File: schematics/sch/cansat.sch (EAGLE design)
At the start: 39 parts

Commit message: cansat main board
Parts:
- removed BAT1IN5V, BAT1INGND, BAT1OUT+, BAT1OUTGND, BAT2IN5V, BAT2INGND, BAT2OUT+, BAT2OUTGND: (no value), pinhead:PINHD-1X1
- removed EXGPIO, EXSPI: (no value), pinhead:PINHD-1X4
- removed EXI2C, EXP1, EXP2, EXP3, EXUART: (no value), pinhead:PINHD-1X2
- removed GPSL: (no value), pinhead:PINHD-1X8
- removed USB: (no value), pinhead:PINHD-1X5
- added D1, D2: GF1, diode:GF1
- added GPS: (no value), pinhead:PINHD-1X4
- added SJ1, SJ2: (no value), jumper:SJ2WW
- C1, C2, C3, C4, C5, C6: device resistor:C-EU025-025X050 -> eagle-ltspice:CC1206
- R1, R2, R3, R4: value (none) -> 10k; device resistor:R-EU_0204/2V -> eagle-ltspice:RR1206
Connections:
- removed net USB5V: BAT1IN5V.1, BAT2IN5V.1, USB.1
- new net ENCODER1_ADC: SJ1.3, VOLTMETER.9
- new net ENCODER1_DIR: RASPIZERO.GPIO20, SJ1.1
- new net ENCODER2_ADC: SJ2.3, VOLTMETER.10
- new net ENCODER2_DIR: RASPIZERO.GPIO21, SJ2.1
- new net N$10: BATIN.1, D1.A
- new net N$11: BATIN.2, D2.A
- new net R_INT: RADIOR.3
- net 3.3V: now also 3.3V1.4, 3.3V2.4, GPS.2; no longer 3.3V1.1, 3.3V2.1, EXP1.1, EXP2.1, EXP3.1, GPSL.7
- net BAT1+: now also 3.3V1.2, D1.C; no longer 3.3V1.3, BAT1OUT+.1, BATIN.1
- net BAT2+: now also 3.3V2.2, D2.C; no longer 3.3V2.3, BAT2OUT+.1, BATIN.2
- net ENCODER1: now also SJ1.2; no longer RASPIZERO.GPIO20
- net ENCODER2: now also SJ2.2; no longer RASPIZERO.GPIO21
- net EX1: no longer EXGPIO.1
- net EX2: no longer EXGPIO.2
- net EX3: no longer EXGPIO.3
- net EX4: no longer EXGPIO.4
- net GND: now also 3.3V1.3, 3.3V2.3, GPS.1, R2.1; no longer 3.3V1.2, 3.3V2.2, BAT1INGND.1, BAT1OUTGND.1, BAT2INGND.1, BAT2OUTGND.1, EXP1.2, EXP2.2, EXP3.2, GPSL.8, USB.5, VOLTMETER.10, VOLTMETER.8
- net GPSTX: now also GPS.3; no longer GPSL.6
- net MISO: no longer EXSPI.1
- net MOSI: no longer EXSPI.2
- net N$1: now also R2.2, VOLTMETER.8; no longer R2.1, VOLTMETER.7
- net N$9: now also VOLTMETER.7; no longer VOLTMETER.9
- net RX: no longer EXUART.2
- net SCL: no longer EXI2C.2
- net SCLK: no longer EXSPI.3
- net SDA: no longer EXI2C.1
- net SHDN: now also 3.3V1.1, 3.3V2.1; no longer 3.3V1.4, 3.3V2.4
- net SS: no longer EXSPI.4
- net TX: no longer EXUART.1
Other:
- note removed: "BATTERY 1 CHARGER"
- note removed: "BATTERY 2 CHARGER"
- note removed: "CHARGERS"
- note removed: "USB INPUT"
- moved on the sheet: BATIN, R1, R2, R3, R4, RADIOR, VOLTMETER

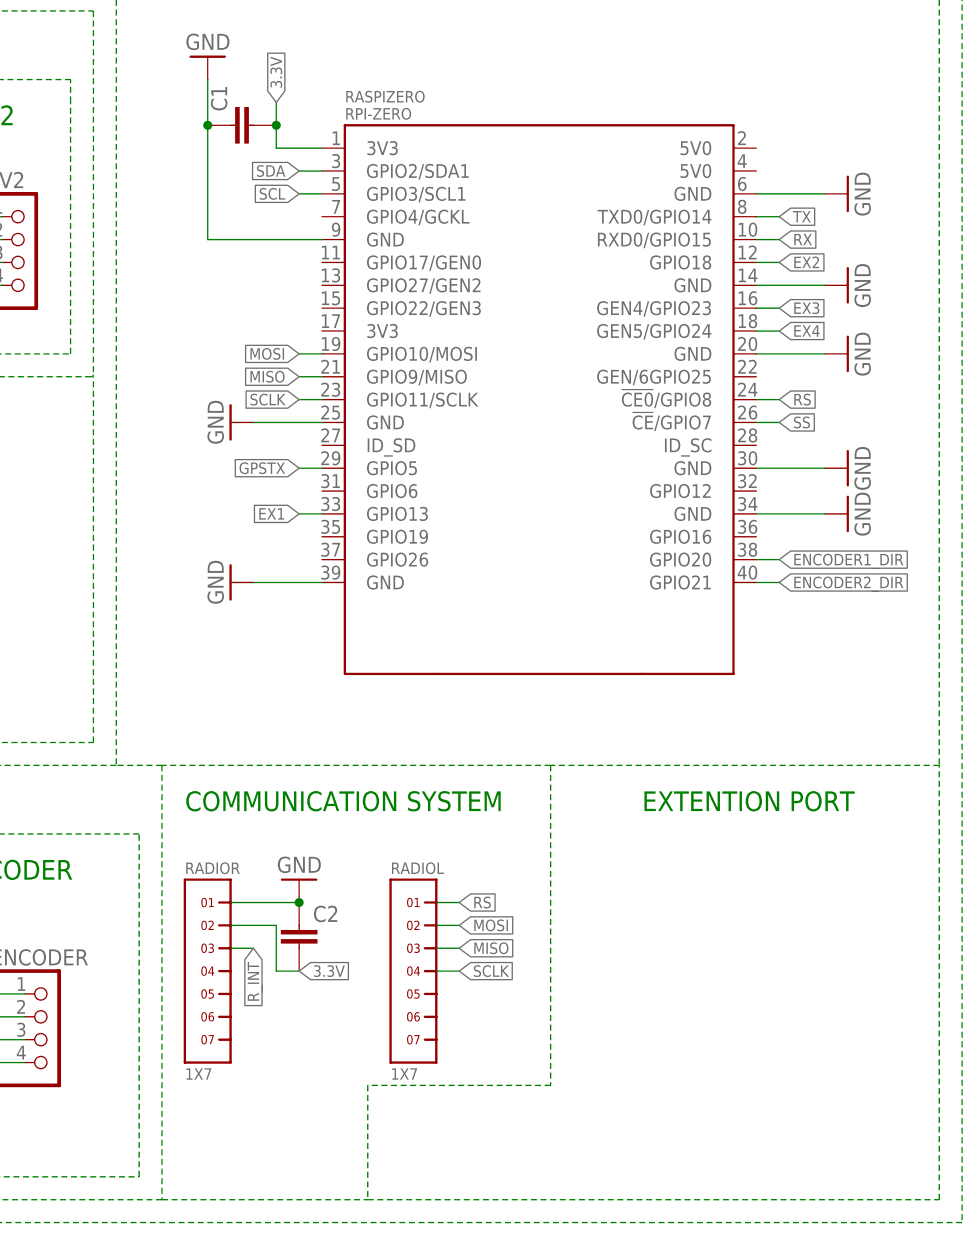
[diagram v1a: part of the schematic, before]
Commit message: cansat board fixed
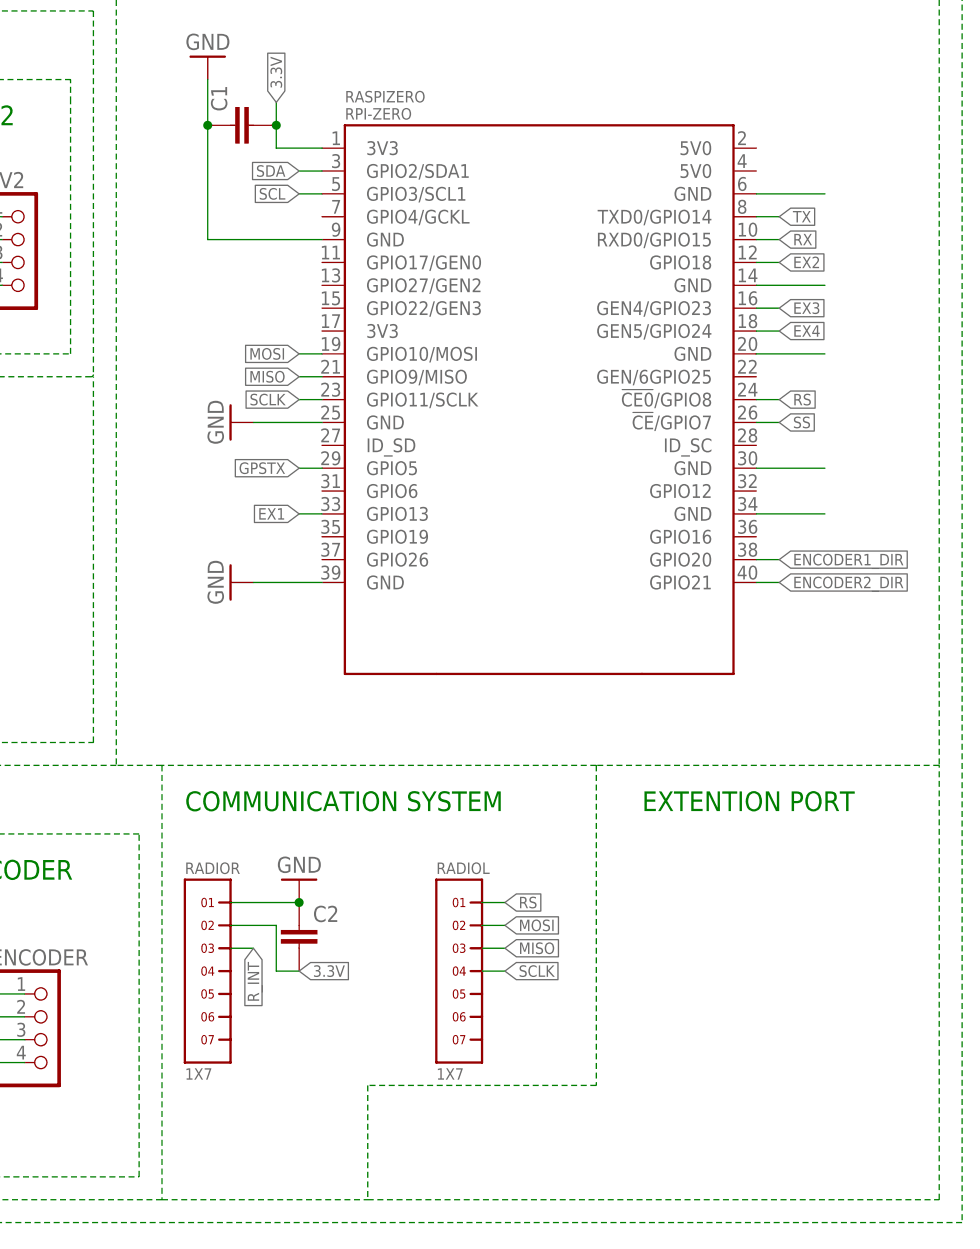
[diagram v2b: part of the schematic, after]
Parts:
- SJ1, SJ2: device jumper:SJ2WW -> jumper:SJ2W
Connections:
- new net GND@4: RASPIZERO.GND@4
- new net GND@5: RASPIZERO.GND@5
- new net GND@6: RASPIZERO.GND@6
- new net GND@7: RASPIZERO.GND@7
- new net GND@8: RASPIZERO.GND@8
- net GND: no longer RASPIZERO.GND@4, RASPIZERO.GND@5, RASPIZERO.GND@6, RASPIZERO.GND@7, RASPIZERO.GND@8
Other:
- moved on the sheet: RADIOL

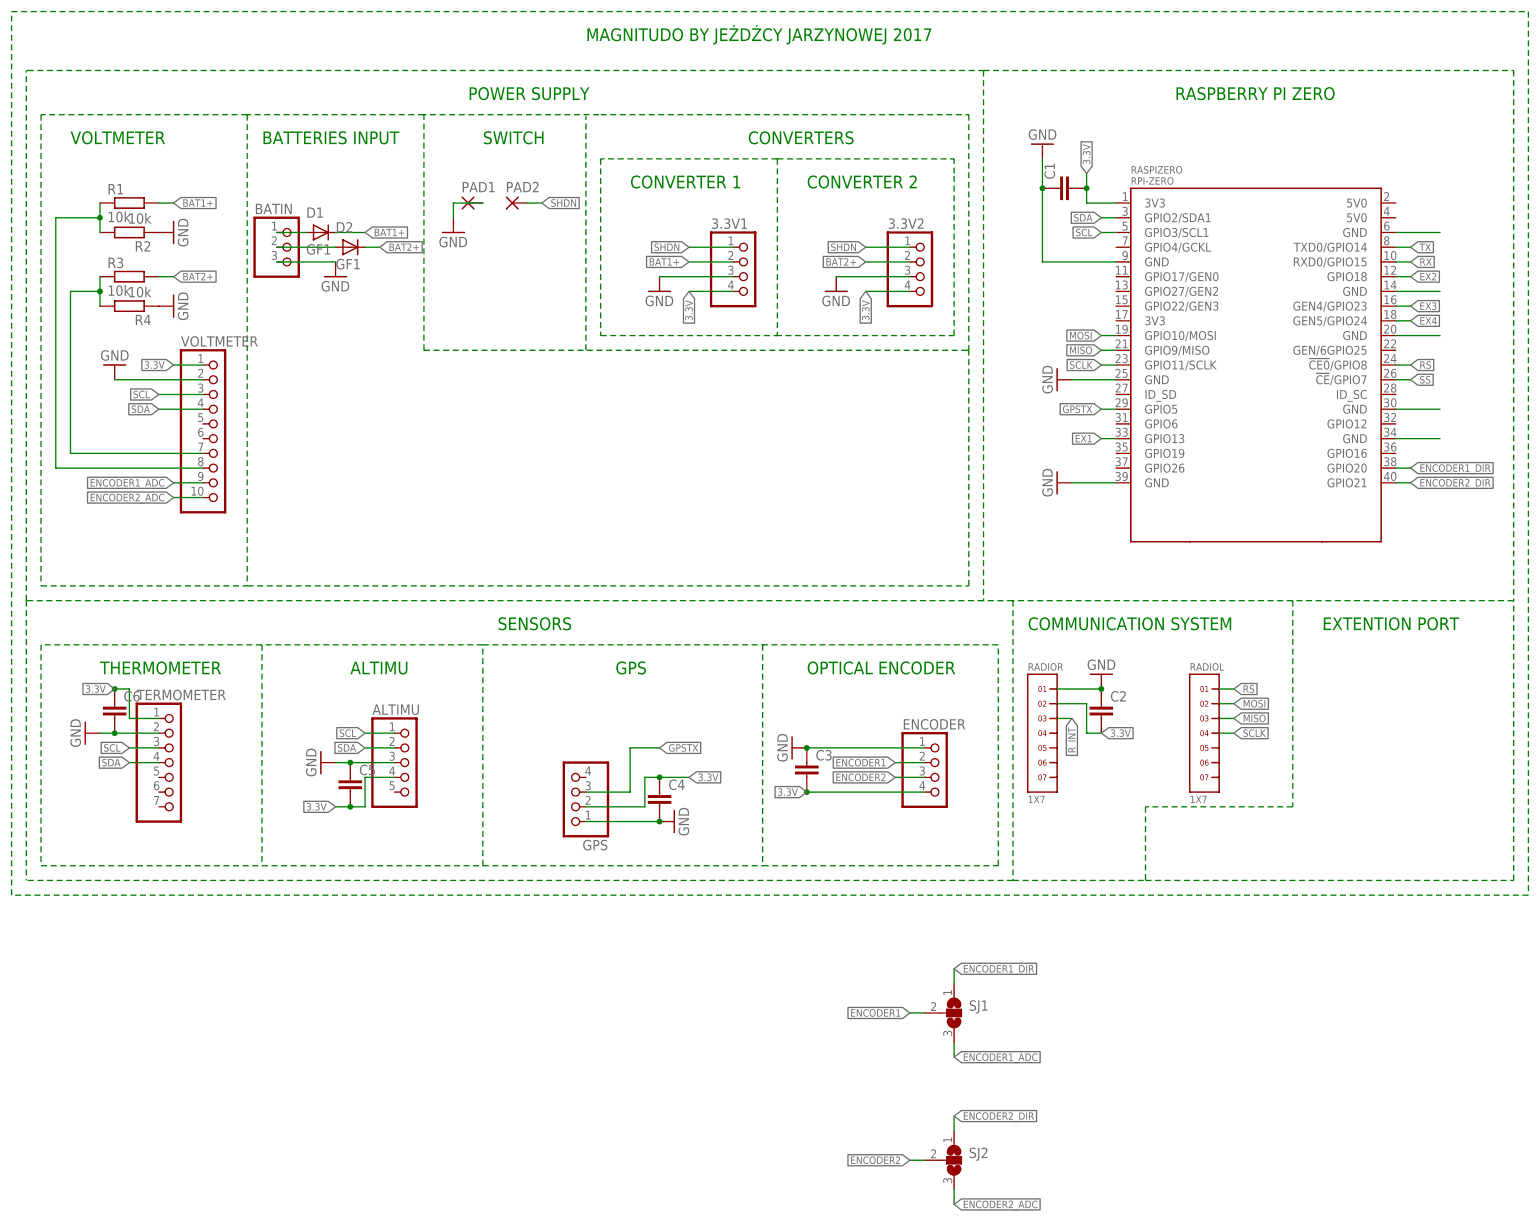
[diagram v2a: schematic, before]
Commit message: optocoupler on radio/gps vcc
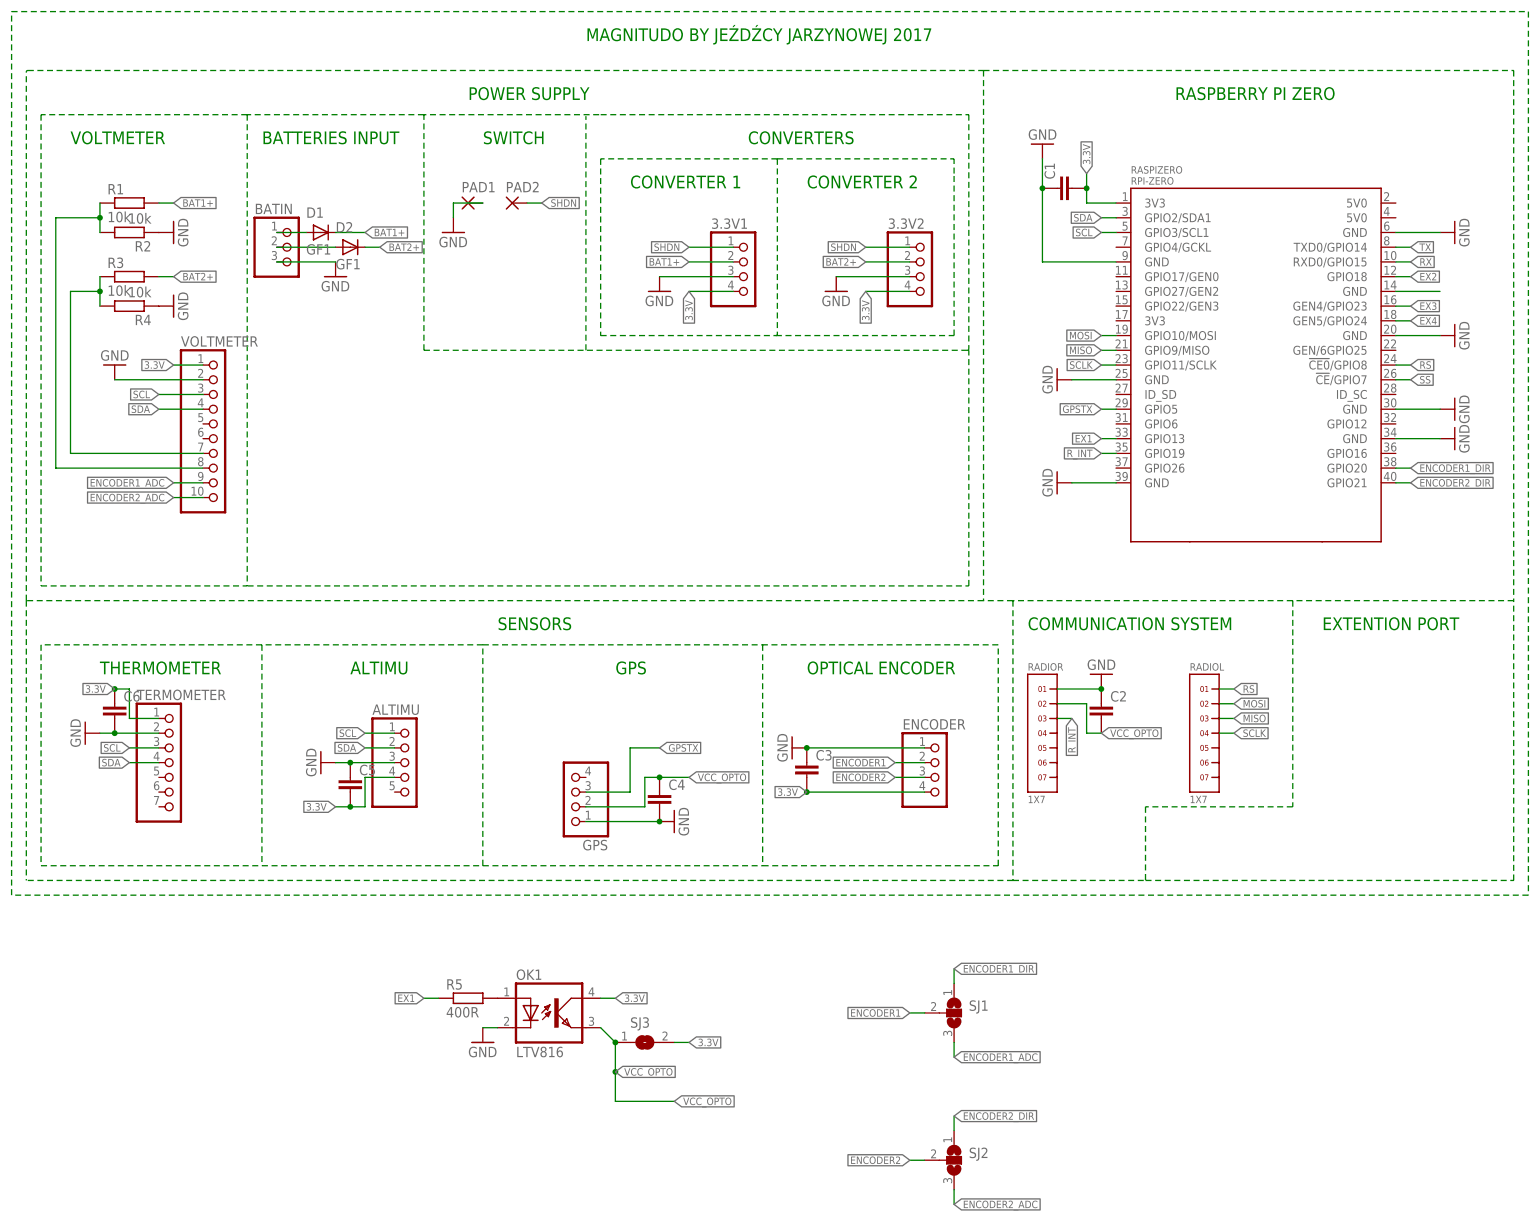
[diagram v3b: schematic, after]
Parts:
- added OK1: LTV816, optocoupler:LTV816
- added R5: 400R, eagle-ltspice:RR1206
- added SJ3: (no value), jumper:SJ
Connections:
- removed net GND@5: RASPIZERO.GND@5
- removed net GND@6: RASPIZERO.GND@6
- removed net GND@7: RASPIZERO.GND@7
- removed net GND@8: RASPIZERO.GND@8
- new net N$2: OK1.A, R5.2
- new net VCC_OPTO: C2.2, C4.1, GPS.2, OK1.EMIT, RADIOR.2, SJ3.1
- net 3.3V: now also OK1.COL, SJ3.2; no longer C2.2, C4.1, GPS.2, RADIOR.2
- net EX1: now also R5.1
- net GND: now also OK1.C, RASPIZERO.GND@5, RASPIZERO.GND@6, RASPIZERO.GND@7, RASPIZERO.GND@8
- net R_INT: now also RASPIZERO.GPIO19
